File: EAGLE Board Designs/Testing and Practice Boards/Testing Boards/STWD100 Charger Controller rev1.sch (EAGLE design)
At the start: 7 parts

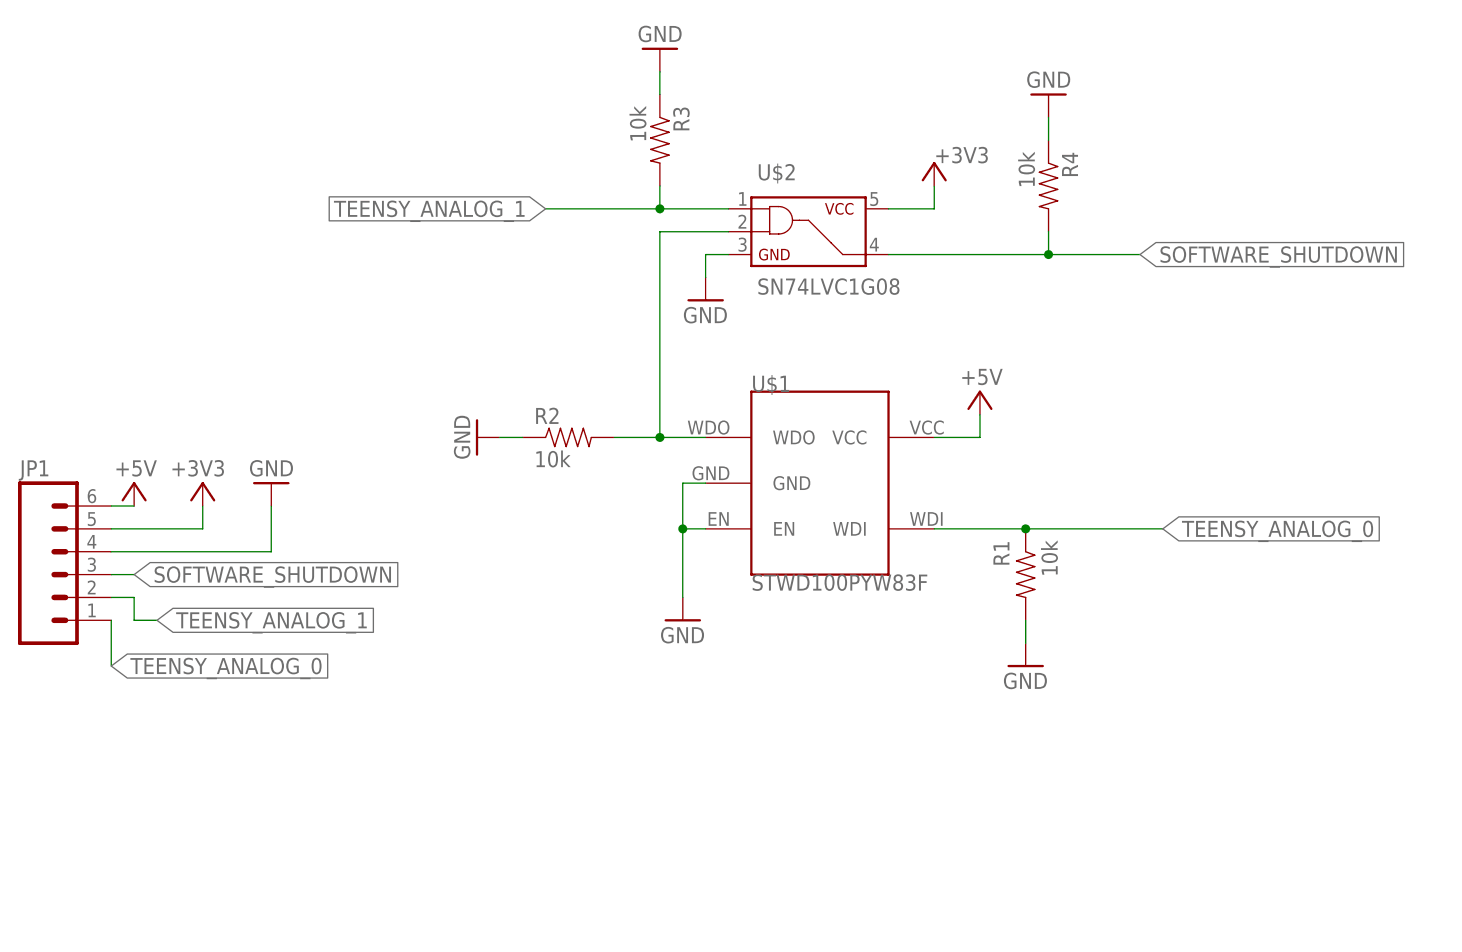
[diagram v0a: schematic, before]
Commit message: add led for WATCHDOG_OK signal
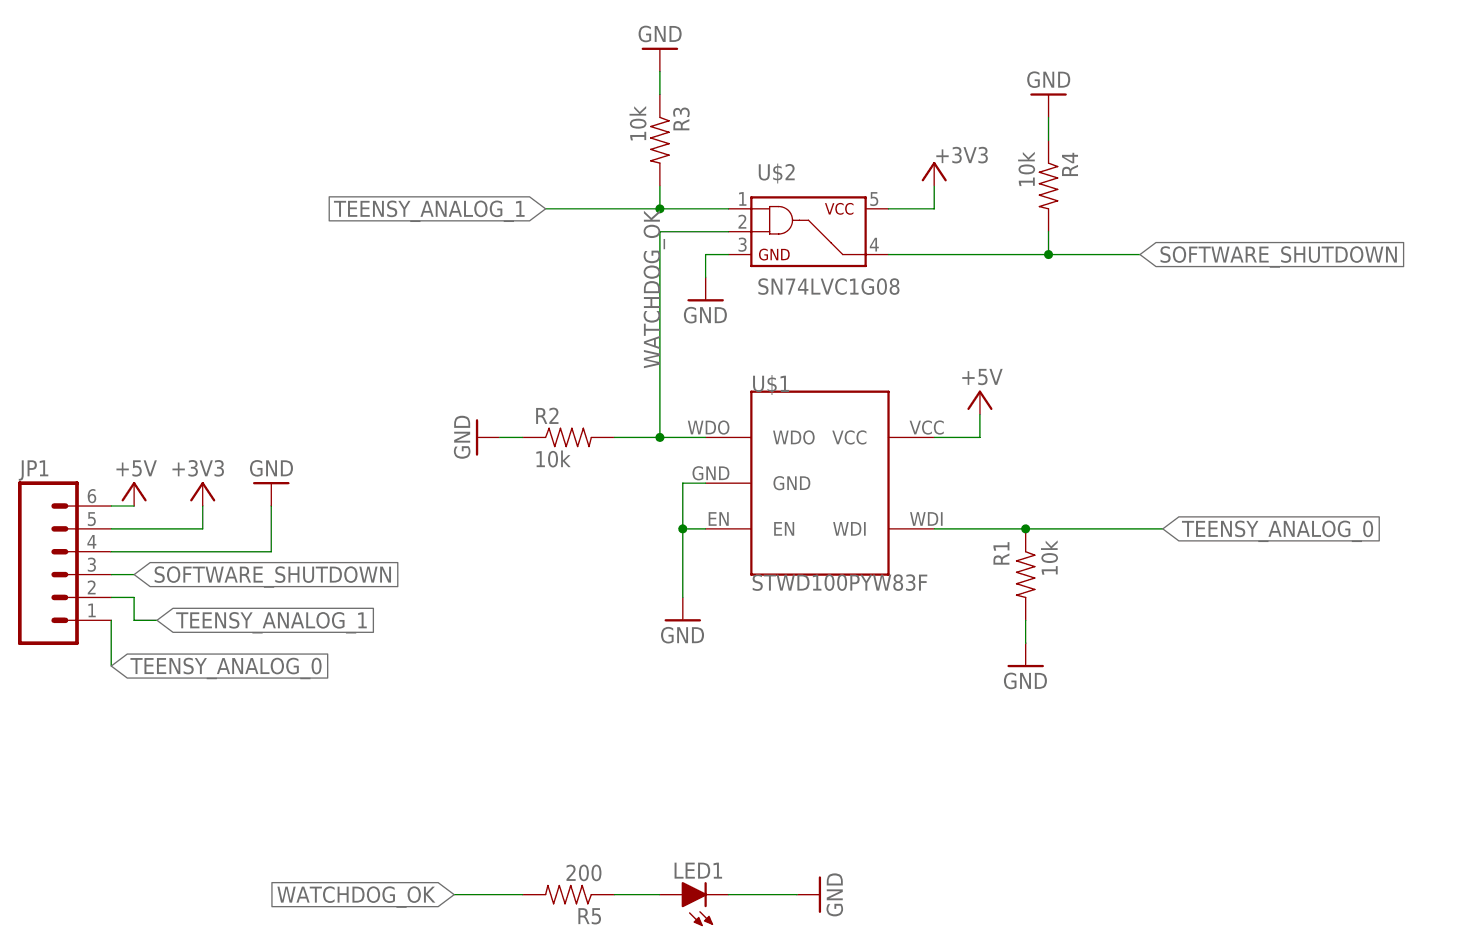
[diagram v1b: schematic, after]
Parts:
- added LED1: (no value), HyTechDevices:LED-0603
- added R5: 200, HyTechDevices:RESISTOR0603-RES
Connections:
- removed net N$2: R2.2, U$1.WDO, U$2.2
- new net N$1: LED1.A, R5.1
- new net WATCHDOG_OK: R2.2, R5.2, U$1.WDO, U$2.2
- net GND: now also LED1.C
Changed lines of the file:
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@@
 <part name="+3V2" library="HyTechSupplies" deviceset="+3V3" device=""/>
 <part name="GND7" library="HyTechSupplies" deviceset="GND" device=""/>
+<part name="GND8" library="HyTechSupplies" deviceset="GND" device=""/>
+<part name="R5" library="HyTechDevices" deviceset="RESISTOR" device="0603-RES" value="200"/>
+<part name="LED1" library="HyTechDevices" deviceset="LED" device="-0603"/>
 </parts>
 <sheets>
@@
 <attribute name="VALUE" x="-53.34" y="5.08" size="1.778" layer="96" rot="R180"/>
 </instance>
+<instance part="GND8" gate="1" x="5.08" y="-43.18" smashed="yes" rot="R90">
+<attribute name="VALUE" x="7.62" y="-45.72" size="1.778" layer="96" rot="R90"/>
+</instance>
+<instance part="R5" gate="G$1" x="-22.86" y="-43.18" smashed="yes" rot="R180">
+<attribute name="NAME" x="-19.05" y="-44.6786" size="1.778" layer="95" rot="R180"/>
+<attribute name="VALUE" x="-19.05" y="-39.878" size="1.778" layer="96" rot="R180"/>
+</instance>
+<instance part="LED1" gate="LED" x="-10.16" y="-43.18" smashed="yes" rot="R90">
+<attribute name="NAME" x="-5.588" y="-39.624" size="1.778" layer="95" rot="R180"/>
+<attribute name="VALUE" x="-5.588" y="-37.465" size="1.778" layer="96" rot="R180"/>
+</instance>
 </instances>
 <busses>
@@
 <wire x1="-55.88" y1="-5.08" x2="-55.88" y2="0" width="0.1524" layer="91"/>
 </segment>
+<segment>
+<pinref part="LED1" gate="LED" pin="C"/>
+<pinref part="GND8" gate="1" pin="GND"/>
+<wire x1="-5.08" y1="-43.18" x2="2.54" y2="-43.18" width="0.1524" layer="91"/>
+</segment>
 </net>
 <net name="+5V" class="0">
@@
 </segment>
 </net>
-<net name="N$2" class="0">
+<net name="WATCHDOG_OK" class="0">
 <segment>
 <pinref part="U$1" gate="G$1" pin="WDO"/>
@@
 <wire x1="-17.78" y1="7.62" x2="-12.7" y2="7.62" width="0.1524" layer="91"/>
 <junction x="-12.7" y="7.62"/>
+<label x="-12.7" y="15.24" size="1.778" layer="95" rot="R90"/>
+</segment>
+<segment>
+<wire x1="-35.56" y1="-43.18" x2="-27.94" y2="-43.18" width="0.1524" layer="91"/>
+<label x="-35.56" y="-43.18" size="1.778" layer="95" rot="R180" xref="yes"/>
+<pinref part="R5" gate="G$1" pin="2"/>
 </segment>
 </net>
@@
 </segment>
 </net>
+<net name="N$1" class="0">
+<segment>
+<pinref part="R5" gate="G$1" pin="1"/>
+<wire x1="-17.78" y1="-43.18" x2="-12.7" y2="-43.18" width="0.1524" layer="91"/>
+<pinref part="LED1" gate="LED" pin="A"/>
+</segment>
+</net>

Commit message: replace 5V with 3V3 and create board
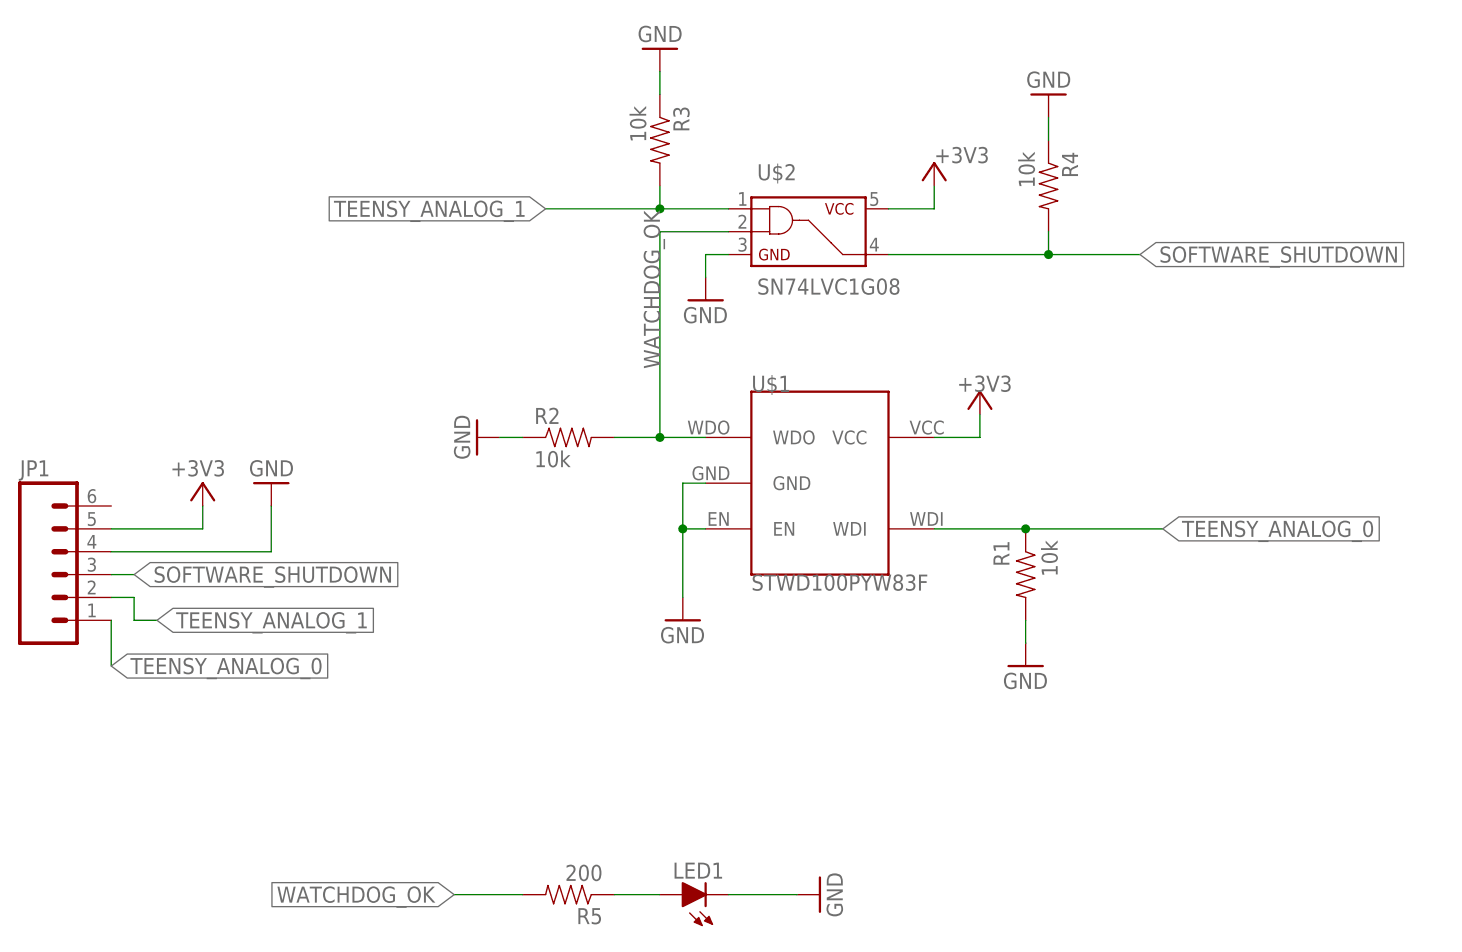
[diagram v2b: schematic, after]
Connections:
- removed net +5V: JP1.6, U$1.VCC
- net +3V3: now also U$1.VCC
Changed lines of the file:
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@@
 <part name="U$2" library="HyTechDevices" deviceset="SN74LVC1G08" device=""/>
 <part name="GND1" library="HyTechSupplies" deviceset="GND" device=""/>
-<part name="P+1" library="HyTechSupplies" deviceset="+5V" device=""/>
 <part name="GND2" library="HyTechSupplies" deviceset="GND" device=""/>
 <part name="GND3" library="HyTechSupplies" deviceset="GND" device=""/>
@@
 <part name="GND6" library="HyTechSupplies" deviceset="GND" device=""/>
 <part name="R4" library="HyTechDevices" deviceset="RESISTOR" device="0603-RES" value="10k"/>
-<part name="P+2" library="HyTechSupplies" deviceset="+5V" device=""/>
 <part name="+3V2" library="HyTechSupplies" deviceset="+3V3" device=""/>
 <part name="GND7" library="HyTechSupplies" deviceset="GND" device=""/>
@@
 <part name="R5" library="HyTechDevices" deviceset="RESISTOR" device="0603-RES" value="200"/>
 <part name="LED1" library="HyTechDevices" deviceset="LED" device="-0603"/>
+<part name="+3V3" library="HyTechSupplies" deviceset="+3V3" device=""/>
 </parts>
 <sheets>
@@
 <attribute name="VALUE" x="-12.7" y="-15.24" size="1.778" layer="96"/>
 </instance>
-<instance part="P+1" gate="1" x="22.86" y="12.7" smashed="yes">
-<attribute name="VALUE" x="25.4" y="15.24" size="1.778" layer="96" rot="R180"/>
-</instance>
 <instance part="GND2" gate="1" x="27.94" y="-17.78" smashed="yes">
 <attribute name="VALUE" x="25.4" y="-20.32" size="1.778" layer="96"/>
@@
 <attribute name="VALUE" x="27.178" y="39.37" size="1.778" layer="96" rot="R270"/>
 </instance>
-<instance part="P+2" gate="1" x="-71.12" y="2.54" smashed="yes">
-<attribute name="VALUE" x="-68.58" y="5.08" size="1.778" layer="96" rot="R180"/>
-</instance>
 <instance part="+3V2" gate="G$1" x="-63.5" y="2.54" smashed="yes">
 <attribute name="VALUE" x="-60.96" y="5.08" size="1.778" layer="96" align="top-right"/>
@@
 <attribute name="NAME" x="-5.588" y="-39.624" size="1.778" layer="95" rot="R180"/>
 <attribute name="VALUE" x="-5.588" y="-37.465" size="1.778" layer="96" rot="R180"/>
+</instance>
+<instance part="+3V3" gate="G$1" x="22.86" y="12.7" smashed="yes">
+<attribute name="VALUE" x="20.32" y="12.7" size="1.778" layer="96"/>
 </instance>
 </instances>
@@
 <pinref part="GND8" gate="1" pin="GND"/>
 <wire x1="-5.08" y1="-43.18" x2="2.54" y2="-43.18" width="0.1524" layer="91"/>
-</segment>
-</net>
-<net name="+5V" class="0">
-<segment>
-<pinref part="P+1" gate="1" pin="+5V"/>
-<wire x1="22.86" y1="10.16" x2="22.86" y2="7.62" width="0.1524" layer="91"/>
-<pinref part="U$1" gate="G$1" pin="VCC"/>
-<wire x1="22.86" y1="7.62" x2="17.78" y2="7.62" width="0.1524" layer="91"/>
-</segment>
-<segment>
-<pinref part="JP1" gate="G$1" pin="6"/>
-<wire x1="-73.66" y1="0" x2="-71.12" y2="0" width="0.1524" layer="91"/>
-<pinref part="P+2" gate="1" pin="+5V"/>
 </segment>
 </net>
@@
 <wire x1="-63.5" y1="-2.54" x2="-63.5" y2="0" width="0.1524" layer="91"/>
 </segment>
-</net>
+<segment>
+<wire x1="22.86" y1="10.16" x2="22.86" y2="7.62" width="0.1524" layer="91"/>
+<pinref part="U$1" gate="G$1" pin="VCC"/>
+<wire x1="22.86" y1="7.62" x2="17.78" y2="7.62" width="0.1524" layer="91"/>
+<pinref part="+3V3" gate="G$1" pin="+3V3"/>
+</segment>
+</net>
